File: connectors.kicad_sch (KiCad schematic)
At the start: 4 parts

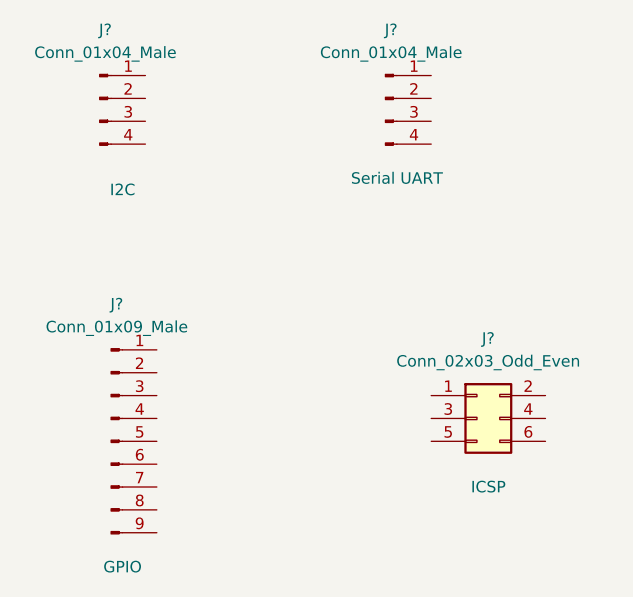
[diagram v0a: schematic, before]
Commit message: Place the symbols at relevent place.(Arrange) and Annote them.
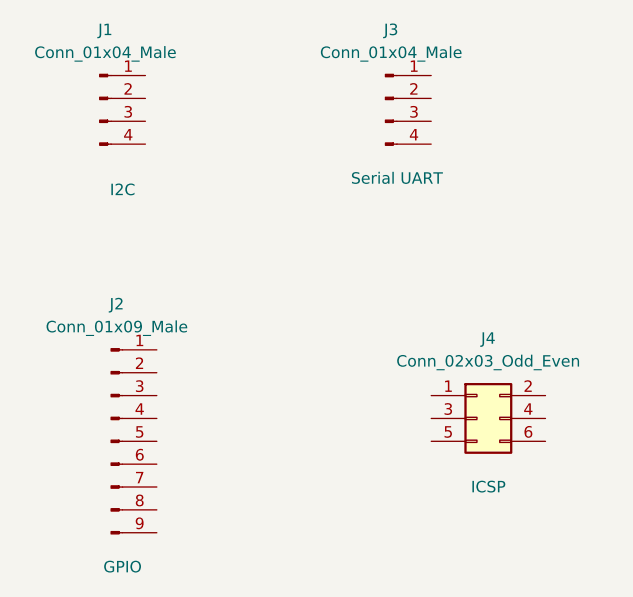
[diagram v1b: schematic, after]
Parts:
- gave numbers to parts that had none: 4
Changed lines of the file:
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@@
   (symbol (lib_id "Connector:Conn_01x04_Male") (at 163.83 67.31 0) (unit 1)
     (in_bom yes) (on_board yes)
-    (property "Reference" "J?" (id 0) (at 164.465 59.69 0))
+    (property "Reference" "J3" (id 0) (at 164.465 59.69 0))
     (property "Value" "Conn_01x04_Male" (id 1) (at 164.465 62.23 0))
     (property "Footprint" "" (id 2) (at 163.83 67.31 0)
@@
   (symbol (lib_id "Connector:Conn_01x04_Male") (at 132.08 67.31 0) (unit 1)
     (in_bom yes) (on_board yes)
-    (property "Reference" "J?" (id 0) (at 132.715 59.69 0))
+    (property "Reference" "J1" (id 0) (at 132.715 59.69 0))
     (property "Value" "Conn_01x04_Male" (id 1) (at 132.715 62.23 0))
     (property "Footprint" "" (id 2) (at 132.08 67.31 0)
@@
   (symbol (lib_id "Connector:Conn_01x09_Male") (at 133.35 105.41 0) (unit 1)
     (in_bom yes) (on_board yes)
-    (property "Reference" "J?" (id 0) (at 133.985 90.17 0))
+    (property "Reference" "J2" (id 0) (at 133.985 90.17 0))
     (property "Value" "Conn_01x09_Male" (id 1) (at 133.985 92.71 0))
     (property "Footprint" "" (id 2) (at 133.35 105.41 0)
@@
   (symbol (lib_id "Connector_Generic:Conn_02x03_Odd_Even") (at 173.99 102.87 0) (unit 1)
     (in_bom yes) (on_board yes)
-    (property "Reference" "J?" (id 0) (at 175.26 93.98 0))
+    (property "Reference" "J4" (id 0) (at 175.26 93.98 0))
     (property "Value" "Conn_02x03_Odd_Even" (id 1) (at 175.26 96.52 0))
     (property "Footprint" "" (id 2) (at 173.99 102.87 0)

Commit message: Done with the symbol-footprint associations
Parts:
- J1, J3: footprint (none) -> Connector_PinHeader_2.54mm:PinHeader_1x04_P2.54mm_Vertical
- J2: footprint (none) -> Connector_PinHeader_2.54mm:PinHeader_1x09_P2.54mm_Vertical
- J4: footprint (none) -> Connector_PinHeader_2.54mm:PinHeader_2x03_P2.54mm_Vertical
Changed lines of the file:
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@@
     (property "Reference" "J3" (id 0) (at 164.465 59.69 0))
     (property "Value" "Conn_01x04_Male" (id 1) (at 164.465 62.23 0))
-    (property "Footprint" "" (id 2) (at 163.83 67.31 0)
+    (property "Footprint" "Connector_PinHeader_2.54mm:PinHeader_1x04_P2.54mm_Vertical" (id 2) (at 163.83 67.31 0)
       (effects (font (size 1.27 1.27)) hide)
     )
@@
     (property "Reference" "J1" (id 0) (at 132.715 59.69 0))
     (property "Value" "Conn_01x04_Male" (id 1) (at 132.715 62.23 0))
-    (property "Footprint" "" (id 2) (at 132.08 67.31 0)
+    (property "Footprint" "Connector_PinHeader_2.54mm:PinHeader_1x04_P2.54mm_Vertical" (id 2) (at 132.08 67.31 0)
       (effects (font (size 1.27 1.27)) hide)
     )
@@
     (property "Reference" "J2" (id 0) (at 133.985 90.17 0))
     (property "Value" "Conn_01x09_Male" (id 1) (at 133.985 92.71 0))
-    (property "Footprint" "" (id 2) (at 133.35 105.41 0)
+    (property "Footprint" "Connector_PinHeader_2.54mm:PinHeader_1x09_P2.54mm_Vertical" (id 2) (at 133.35 105.41 0)
       (effects (font (size 1.27 1.27)) hide)
     )
@@
     (property "Reference" "J4" (id 0) (at 175.26 93.98 0))
     (property "Value" "Conn_02x03_Odd_Even" (id 1) (at 175.26 96.52 0))
-    (property "Footprint" "" (id 2) (at 173.99 102.87 0)
+    (property "Footprint" "Connector_PinHeader_2.54mm:PinHeader_2x03_P2.54mm_Vertical" (id 2) (at 173.99 102.87 0)
       (effects (font (size 1.27 1.27)) hide)
     )

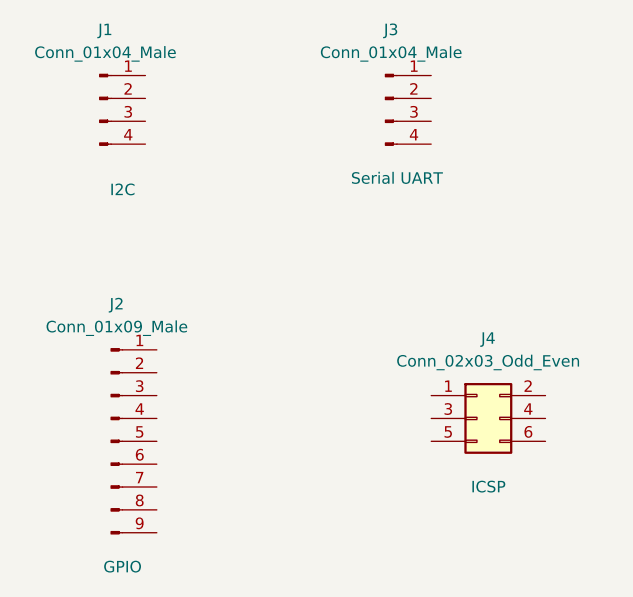
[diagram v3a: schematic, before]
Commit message: Completed the wiring of Connectors sheet(2). PS: No ERC error.
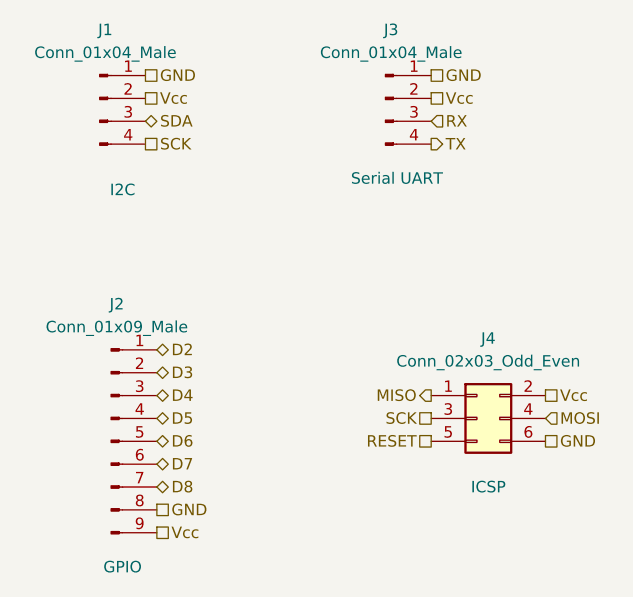
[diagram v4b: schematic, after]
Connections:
- net GND: now reaches J3.1 (Pin_1)
- net GND: now also J1.1 (Pin_1), J2.8 (Pin_8), J4.6 (Pin_6)
- net Vcc: now reaches J3.2 (Pin_2)
- net Vcc: now also J1.2 (Pin_2), J2.9 (Pin_9), J4.2 (Pin_2)
- net RX: now reaches J3.3 (Pin_3)
- net TX: now reaches J3.4 (Pin_4)
- net SDA: now reaches J1.3 (Pin_3)
- net SCK: now reaches J1.4 (Pin_4)
- net SCK: now also J4.3 (Pin_3)
- net D2: now reaches J2.1 (Pin_1)
- net D3: now reaches J2.2 (Pin_2)
- net D4: now reaches J2.3 (Pin_3)
- net D5: now reaches J2.4 (Pin_4)
- net D6: now reaches J2.5 (Pin_5)
- net D7: now reaches J2.6 (Pin_6)
- net D8: now reaches J2.7 (Pin_7)
- net MISO: now reaches J4.1 (Pin_1)
- net MOSI: now reaches J4.4 (Pin_4)
- net RESET: now reaches J4.5 (Pin_5)
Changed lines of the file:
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@@
 (kicad_sch (version 20211123) (generator eeschema)
   (paper "A4")
+  (hierarchical_label "D6" (shape bidirectional) (at 138.43 105.41 0)
+    (effects (font (size 1.27 1.27)) (justify left))
+  )
+  (hierarchical_label "Vcc" (shape passive) (at 181.61 100.33 0)
+    (effects (font (size 1.27 1.27)) (justify left))
+  )
+  (hierarchical_label "RESET" (shape passive) (at 168.91 105.41 180)
+    (effects (font (size 1.27 1.27)) (justify right))
+  )
+  (hierarchical_label "D7" (shape bidirectional) (at 138.43 107.95 0)
+    (effects (font (size 1.27 1.27)) (justify left))
+  )
+  (hierarchical_label "GND" (shape passive) (at 138.43 113.03 0)
+    (effects (font (size 1.27 1.27)) (justify left))
+  )
+  (hierarchical_label "Vcc" (shape passive) (at 138.43 115.57 0)
+    (effects (font (size 1.27 1.27)) (justify left))
+  )
+  (hierarchical_label "D2" (shape bidirectional) (at 138.43 95.25 0)
+    (effects (font (size 1.27 1.27)) (justify left))
+  )
+  (hierarchical_label "MOSI" (shape input) (at 181.61 102.87 0)
+    (effects (font (size 1.27 1.27)) (justify left))
+  )
+  (hierarchical_label "Vcc" (shape passive) (at 137.16 67.31 0)
+    (effects (font (size 1.27 1.27)) (justify left))
+  )
+  (hierarchical_label "SDA" (shape bidirectional) (at 137.16 69.85 0)
+    (effects (font (size 1.27 1.27)) (justify left))
+  )
+  (hierarchical_label "SCK" (shape passive) (at 168.91 102.87 180)
+    (effects (font (size 1.27 1.27)) (justify right))
+  )
+  (hierarchical_label "GND" (shape passive) (at 181.61 105.41 0)
+    (effects (font (size 1.27 1.27)) (justify left))
+  )
+  (hierarchical_label "D4" (shape bidirectional) (at 138.43 100.33 0)
+    (effects (font (size 1.27 1.27)) (justify left))
+  )
+  (hierarchical_label "SCK" (shape passive) (at 137.16 72.39 0)
+    (effects (font (size 1.27 1.27)) (justify left))
+  )
+  (hierarchical_label "RX" (shape input) (at 168.91 69.85 0)
+    (effects (font (size 1.27 1.27)) (justify left))
+  )
+  (hierarchical_label "GND" (shape passive) (at 168.91 64.77 0)
+    (effects (font (size 1.27 1.27)) (justify left))
+  )
+  (hierarchical_label "GND" (shape passive) (at 137.16 64.77 0)
+    (effects (font (size 1.27 1.27)) (justify left))
+  )
+  (hierarchical_label "D8" (shape bidirectional) (at 138.43 110.49 0)
+    (effects (font (size 1.27 1.27)) (justify left))
+  )
+  (hierarchical_label "Vcc" (shape passive) (at 168.91 67.31 0)
+    (effects (font (size 1.27 1.27)) (justify left))
+  )
+  (hierarchical_label "MISO" (shape output) (at 168.91 100.33 180)
+    (effects (font (size 1.27 1.27)) (justify right))
+  )
+  (hierarchical_label "D3" (shape bidirectional) (at 138.43 97.79 0)
+    (effects (font (size 1.27 1.27)) (justify left))
+  )
+  (hierarchical_label "D5" (shape bidirectional) (at 138.43 102.87 0)
+    (effects (font (size 1.27 1.27)) (justify left))
+  )
+  (hierarchical_label "TX" (shape output) (at 168.91 72.39 0)
+    (effects (font (size 1.27 1.27)) (justify left))
+  )
   (symbol (lib_id "Connector:Conn_01x04_Male") (at 163.83 67.31 0) (unit 1)
     (in_bom yes) (on_board yes)
